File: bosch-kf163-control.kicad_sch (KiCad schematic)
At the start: 34 parts, among them J101 TGA, J102 PROG, Q101 DTC143ZE, Q102 DTC143ZE, Q103 DTC143ZE, Q104 DTC143ZE, U101 74HC165D, U102 AMS1117-3.3, U103 ESP32-WROOM-32U

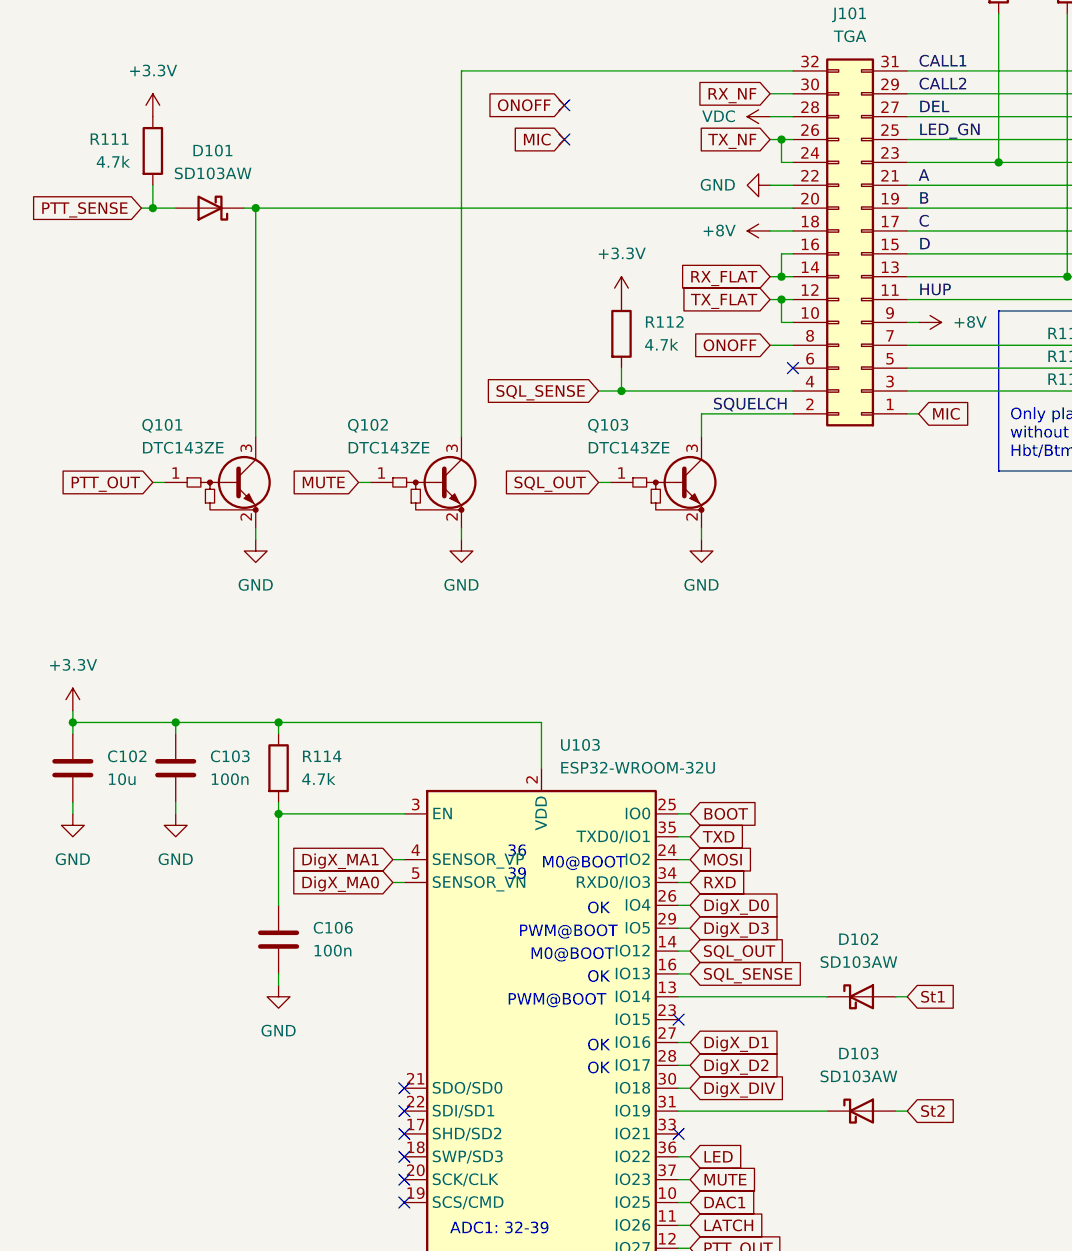
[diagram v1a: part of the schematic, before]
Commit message: silkscreen symbols and text, various schematic/pcb updates
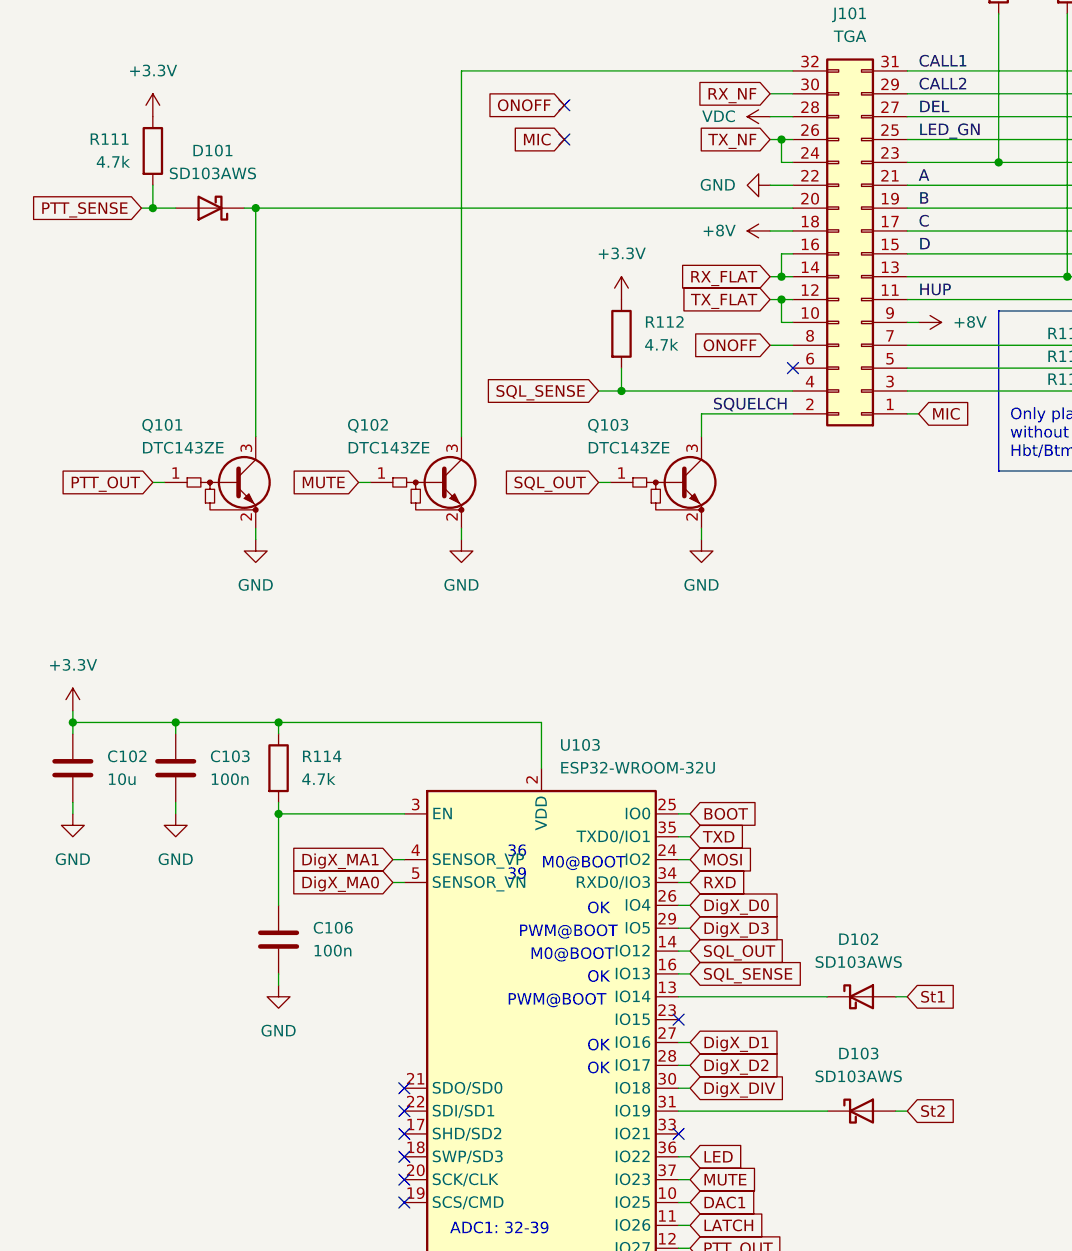
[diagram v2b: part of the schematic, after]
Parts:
- D101, D102, D103: value SD103AW -> SD103AWS; footprint Diode_SMD:D_SOD-123 -> Diode_SMD:D_SOD-323; LCSC C181204 -> C438010
- J102: footprint Connector_PinHeader_2.54mm:PinHeader_1x04_P2.54mm_Horizontal -> Connector_PinHeader_2.54mm:PinHeader_1x04_P2.54mm_Vertical; DNP (none) -> DNP
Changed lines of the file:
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@@
   (title_block
     (title "Bosch KF163 control")
-    (date "2022-01-20")
+    (date "2022-01-21")
     (rev "1")
     (company "Robin Olejnik")
@@
     (in_bom yes) (on_board yes) (fields_autoplaced)
     (property "Reference" "D102" (id 0) (at 131.7625 134.62 0))
-    (property "Value" "SD103AW" (id 1) (at 131.7625 137.16 0))
-    (property "Footprint" "Diode_SMD:D_SOD-123" (id 2) (at 132.08 140.97 0)
-      (effects (font (size 1.27 1.27)) hide)
-    )
-    (property "Datasheet" "https://datasheet.lcsc.com/lcsc/1809211428_Guangdong-Hottech-SD103AW_C181204.pdf" (id 3) (at 132.08 140.97 0)
-      (effects (font (size 1.27 1.27)) hide)
-    )
-    (property "LCSC" "C181204" (id 4) (at 132.08 140.97 0)
+    (property "Value" "SD103AWS" (id 1) (at 131.7625 137.16 0))
+    (property "Footprint" "Diode_SMD:D_SOD-323" (id 2) (at 132.08 140.97 0)
+      (effects (font (size 1.27 1.27)) hide)
+    )
+    (property "Datasheet" "https://datasheet.lcsc.com/lcsc/1912111437_Shandong-Jingdao-Microelectronics-SD103AWS_C438010.pdf" (id 3) (at 132.08 140.97 0)
+      (effects (font (size 1.27 1.27)) hide)
+    )
+    (property "LCSC" "C438010" (id 4) (at 132.08 140.97 0)
       (effects (font (size 1.27 1.27)) hide)
     )
@@
       (effects (font (size 1.27 1.27)) (justify right))
     )
-    (property "Footprint" "Connector_PinHeader_2.54mm:PinHeader_1x04_P2.54mm_Horizontal" (id 2) (at 171.45 148.59 0)
+    (property "Footprint" "Connector_PinHeader_2.54mm:PinHeader_1x04_P2.54mm_Vertical" (id 2) (at 171.45 148.59 0)
       (effects (font (size 1.27 1.27)) hide)
     )
@@
     )
     (property "variant" "Base" (id 4) (at 171.45 148.59 0)
+      (effects (font (size 1.27 1.27)) hide)
+    )
+    (property "DNP" "DNP" (id 5) (at 171.45 148.59 0)
       (effects (font (size 1.27 1.27)) hide)
     )
@@
     (in_bom yes) (on_board yes) (fields_autoplaced)
     (property "Reference" "D101" (id 0) (at 60.0075 46.99 0))
-    (property "Value" "SD103AW" (id 1) (at 60.0075 49.53 0))
-    (property "Footprint" "Diode_SMD:D_SOD-123" (id 2) (at 59.69 53.34 0)
-      (effects (font (size 1.27 1.27)) hide)
-    )
-    (property "Datasheet" "https://datasheet.lcsc.com/lcsc/1809211428_Guangdong-Hottech-SD103AW_C181204.pdf" (id 3) (at 59.69 53.34 0)
-      (effects (font (size 1.27 1.27)) hide)
-    )
-    (property "LCSC" "C181204" (id 4) (at 59.69 53.34 0)
+    (property "Value" "SD103AWS" (id 1) (at 60.0075 49.53 0))
+    (property "Footprint" "Diode_SMD:D_SOD-323" (id 2) (at 59.69 53.34 0)
+      (effects (font (size 1.27 1.27)) hide)
+    )
+    (property "Datasheet" "https://datasheet.lcsc.com/lcsc/1912111437_Shandong-Jingdao-Microelectronics-SD103AWS_C438010.pdf" (id 3) (at 59.69 53.34 0)
+      (effects (font (size 1.27 1.27)) hide)
+    )
+    (property "LCSC" "C438010" (id 4) (at 59.69 53.34 0)
       (effects (font (size 1.27 1.27)) hide)
     )
@@
     (in_bom yes) (on_board yes) (fields_autoplaced)
     (property "Reference" "D103" (id 0) (at 131.7625 147.32 0))
-    (property "Value" "SD103AW" (id 1) (at 131.7625 149.86 0))
-    (property "Footprint" "Diode_SMD:D_SOD-123" (id 2) (at 132.08 153.67 0)
-      (effects (font (size 1.27 1.27)) hide)
-    )
-    (property "Datasheet" "https://datasheet.lcsc.com/lcsc/1809211428_Guangdong-Hottech-SD103AW_C181204.pdf" (id 3) (at 132.08 153.67 0)
-      (effects (font (size 1.27 1.27)) hide)
-    )
-    (property "LCSC" "C181204" (id 4) (at 132.08 153.67 0)
+    (property "Value" "SD103AWS" (id 1) (at 131.7625 149.86 0))
+    (property "Footprint" "Diode_SMD:D_SOD-323" (id 2) (at 132.08 153.67 0)
+      (effects (font (size 1.27 1.27)) hide)
+    )
+    (property "Datasheet" "https://datasheet.lcsc.com/lcsc/1912111437_Shandong-Jingdao-Microelectronics-SD103AWS_C438010.pdf" (id 3) (at 132.08 153.67 0)
+      (effects (font (size 1.27 1.27)) hide)
+    )
+    (property "LCSC" "C438010" (id 4) (at 132.08 153.67 0)
       (effects (font (size 1.27 1.27)) hide)
     )
@@
     )
     (path "/9817064a-82bb-4f74-9ccf-66121bf66e31"
-      (reference "D101") (unit 1) (value "SD103AW") (footprint "Diode_SMD:D_SOD-123")
+      (reference "D101") (unit 1) (value "SD103AWS") (footprint "Diode_SMD:D_SOD-323")
     )
     (path "/0ddf6a51-9768-4bfa-a4e5-dd042e582587"
-      (reference "D102") (unit 1) (value "SD103AW") (footprint "Diode_SMD:D_SOD-123")
+      (reference "D102") (unit 1) (value "SD103AWS") (footprint "Diode_SMD:D_SOD-323")
     )
     (path "/bb33d267-45f6-41b8-b05e-d1ba7c3c8b6a"
-      (reference "D103") (unit 1) (value "SD103AW") (footprint "Diode_SMD:D_SOD-123")
+      (reference "D103") (unit 1) (value "SD103AWS") (footprint "Diode_SMD:D_SOD-323")
     )
     (path "/dede5982-788e-4422-a3af-a7f72e3578e0/c85c7e19-3434-4428-bd93-906044f757ef"
-      (reference "D201") (unit 1) (value "SD103AW") (footprint "Diode_SMD:D_SOD-123")
+      (reference "D201") (unit 1) (value "SD103AWS") (footprint "Diode_SMD:D_SOD-323")
     )
     (path "/dede5982-788e-4422-a3af-a7f72e3578e0/ed4a2a2b-6f1d-4714-816e-8971eefe01e9"
-      (reference "D202") (unit 1) (value "SD103AW") (footprint "Diode_SMD:D_SOD-123")
+      (reference "D202") (unit 1) (value "SD103AWS") (footprint "Diode_SMD:D_SOD-323")
     )
     (path "/dede5982-788e-4422-a3af-a7f72e3578e0/9ba5aa00-0676-4c8f-a481-2061c528c134"
-      (reference "D203") (unit 1) (value "SD103AW") (footprint "Diode_SMD:D_SOD-123")
+      (reference "D203") (unit 1) (value "SD103AWS") (footprint "Diode_SMD:D_SOD-323")
     )
     (path "/dede5982-788e-4422-a3af-a7f72e3578e0/fcc5a85d-9a08-4c38-bac4-ad2522642fae"
-      (reference "D204") (unit 1) (value "SD103AW") (footprint "Diode_SMD:D_SOD-123")
+      (reference "D204") (unit 1) (value "SD103AWS") (footprint "Diode_SMD:D_SOD-323")
     )
     (path "/dede5982-788e-4422-a3af-a7f72e3578e0/3220a727-104c-4433-8710-d227af9735a2"
-      (reference "D205") (unit 1) (value "SD103AW") (footprint "Diode_SMD:D_SOD-123")
+      (reference "D205") (unit 1) (value "SD103AWS") (footprint "Diode_SMD:D_SOD-323")
     )
     (path "/dede5982-788e-4422-a3af-a7f72e3578e0/6ecc950b-ae9d-42fc-8e99-53c00266a2f9"
-      (reference "D206") (unit 1) (value "SD103AW") (footprint "Diode_SMD:D_SOD-123")
+      (reference "D206") (unit 1) (value "SD103AWS") (footprint "Diode_SMD:D_SOD-323")
     )
     (path "/dede5982-788e-4422-a3af-a7f72e3578e0/31219f03-cbc5-42bb-ab29-1b07fdd09aae"
-      (reference "D207") (unit 1) (value "SD103AW") (footprint "Diode_SMD:D_SOD-123")
+      (reference "D207") (unit 1) (value "SD103AWS") (footprint "Diode_SMD:D_SOD-323")
     )
     (path "/dede5982-788e-4422-a3af-a7f72e3578e0/b1b970d7-4c46-41ab-a35d-178263d0dde3"
-      (reference "D208") (unit 1) (value "SD103AW") (footprint "Diode_SMD:D_SOD-123")
+      (reference "D208") (unit 1) (value "SD103AWS") (footprint "Diode_SMD:D_SOD-323")
     )
     (path "/dede5982-788e-4422-a3af-a7f72e3578e0/3d92ed49-6cdf-463b-b61c-0aa682d5bd8a"
-      (reference "D209") (unit 1) (value "SD103AW") (footprint "Diode_SMD:D_SOD-123")
+      (reference "D209") (unit 1) (value "SD103AWS") (footprint "Diode_SMD:D_SOD-323")
     )
     (path "/dede5982-788e-4422-a3af-a7f72e3578e0/b9a026c9-7f71-4c30-92be-6081ea1e28b3"
-      (reference "D210") (unit 1) (value "SD103AW") (footprint "Diode_SMD:D_SOD-123")
+      (reference "D210") (unit 1) (value "SD103AWS") (footprint "Diode_SMD:D_SOD-323")
     )
     (path "/dede5982-788e-4422-a3af-a7f72e3578e0/b670d2cd-2c10-4bb9-af2b-1f24f7467020"
-      (reference "D211") (unit 1) (value "SD103AW") (footprint "Diode_SMD:D_SOD-123")
+      (reference "D211") (unit 1) (value "SD103AWS") (footprint "Diode_SMD:D_SOD-323")
     )
     (path "/dede5982-788e-4422-a3af-a7f72e3578e0/e85e239e-7529-4db9-ab5d-aaa06314d7a8"
-      (reference "D212") (unit 1) (value "SD103AW") (footprint "Diode_SMD:D_SOD-123")
+      (reference "D212") (unit 1) (value "SD103AWS") (footprint "Diode_SMD:D_SOD-323")
     )
     (path "/dede5982-788e-4422-a3af-a7f72e3578e0/938029dd-d3b4-469c-b32c-48394f4ec1e5"
-      (reference "D213") (unit 1) (value "SD103AW") (footprint "Diode_SMD:D_SOD-123")
+      (reference "D213") (unit 1) (value "SD103AWS") (footprint "Diode_SMD:D_SOD-323")
     )
     (path "/dede5982-788e-4422-a3af-a7f72e3578e0/c5bc4b13-6647-4f60-8f48-300afaf06625"
-      (reference "D214") (unit 1) (value "SD103AW") (footprint "Diode_SMD:D_SOD-123")
+      (reference "D214") (unit 1) (value "SD103AWS") (footprint "Diode_SMD:D_SOD-323")
     )
     (path "/ff8439ee-e442-4797-993a-fd9bd2fc0f11"
@@
     )
     (path "/7c8914de-c925-4075-b5b8-1ed116b0d291"
-      (reference "J102") (unit 1) (value "PROG") (footprint "Connector_PinHeader_2.54mm:PinHeader_1x04_P2.54mm_Horizontal")
+      (reference "J102") (unit 1) (value "PROG") (footprint "Connector_PinHeader_2.54mm:PinHeader_1x04_P2.54mm_Vertical")
     )
     (path "/dede5982-788e-4422-a3af-a7f72e3578e0/3faf5fa1-7cc4-4ff7-91c9-bdedff672978"
